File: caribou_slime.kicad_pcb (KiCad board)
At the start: 2 copper layers, 36.1 x 28.4 mm, 12 parts, among them J1 Conn_01x02_MountingPin, U1 ESP32-C3_SUPERMINI, U2 BMI270, U3 TP4056

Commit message: docs(pcb): Update silkscreen version number
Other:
- board text added: "Caribou Slime V1.1 By Pon Pon"
- board text removed: "Caribou Slime V1.0.1 By Pon Pon"
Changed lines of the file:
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@@
   (gr_rect (start 33.274 25.654) (end 69.342 54.102)
     (stroke (width 0.1) (type default)) (fill none) (layer "Edge.Cuts"))
-  (gr_text "Caribou Slime\nV1.0.1\nBy Pon Pon" (at 68.834 42.418) (layer "B.SilkS")
+  (gr_text "Caribou Slime\nV1.1\nBy Pon Pon" (at 68.834 42.418) (layer "B.SilkS")
     (effects (font (size 1 1) (thickness 0.15)) (justify left bottom mirror))
   )

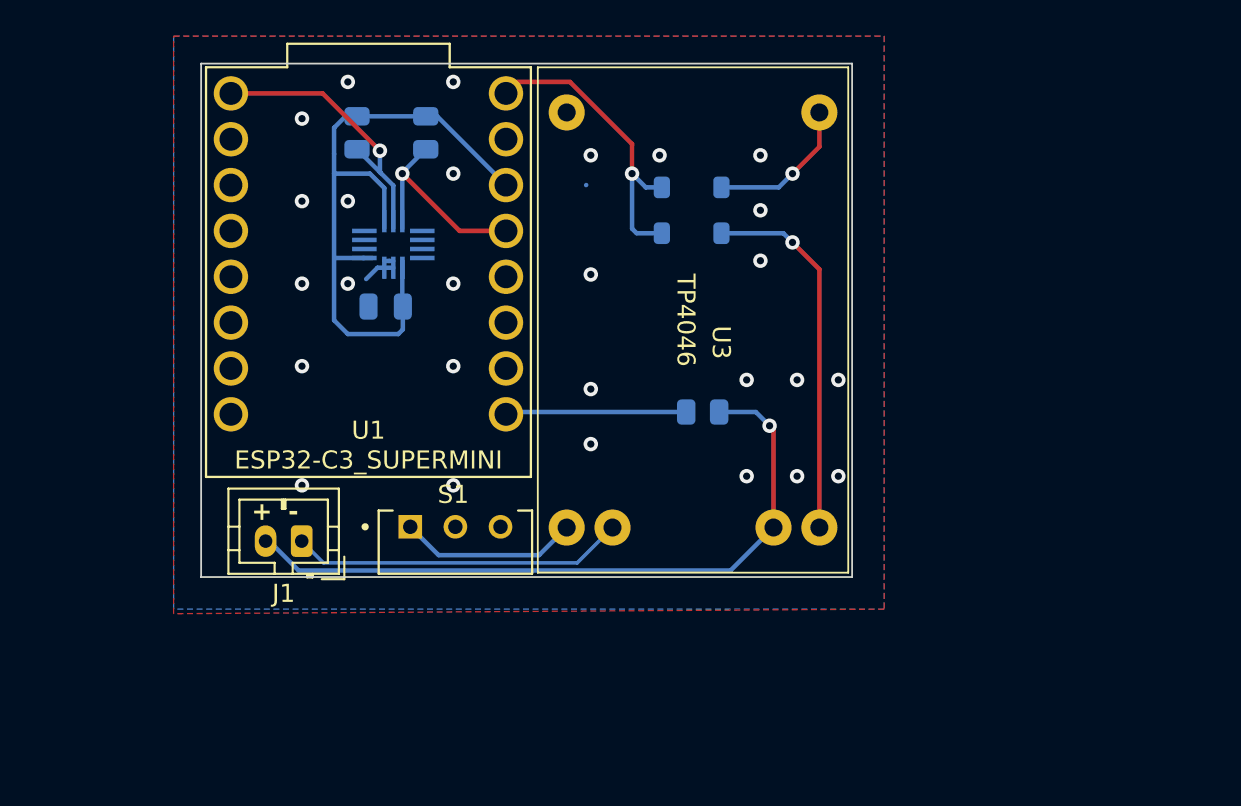
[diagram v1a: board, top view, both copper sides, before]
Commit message: chore(pcb): Remove TP4056 board
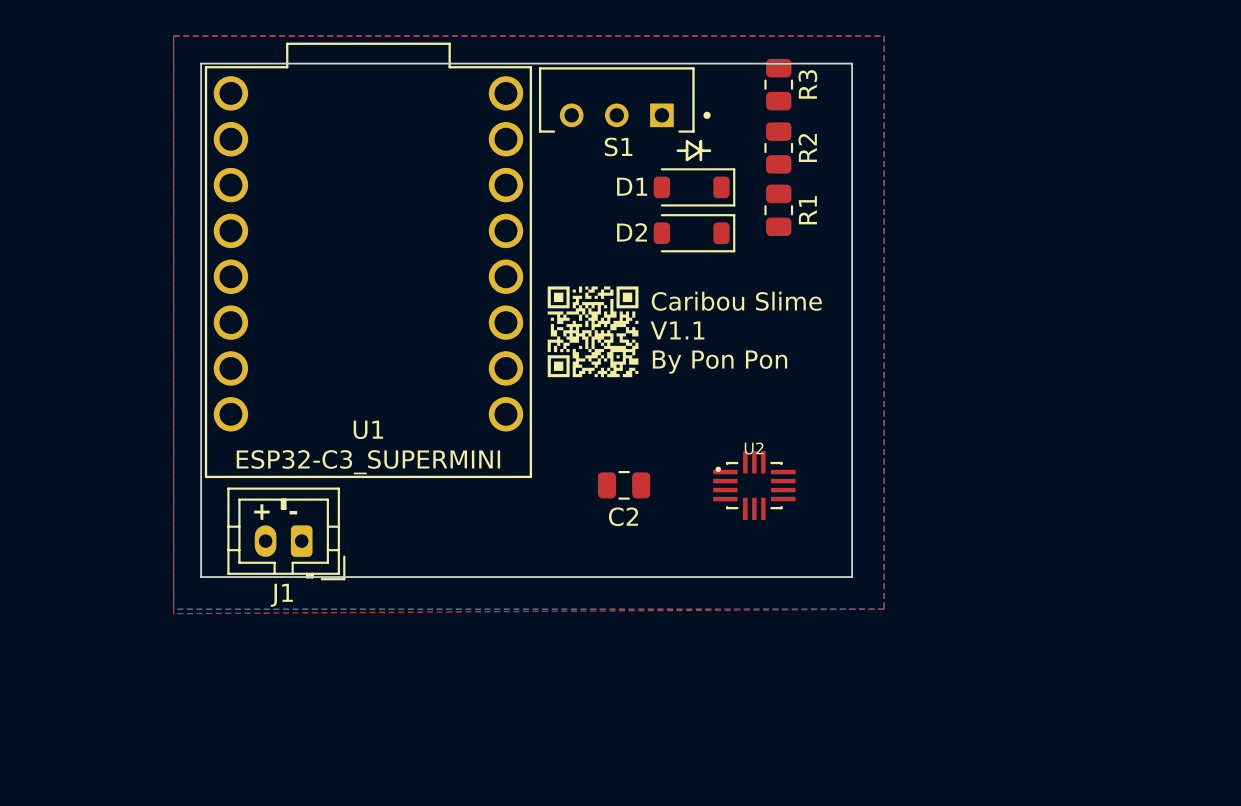
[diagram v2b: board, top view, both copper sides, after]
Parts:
- removed U3: TP4056, TP4056_Charging_Board:TP4056 Charging Board
- C2, D1, D2, G***, R1, R2, R3, U2: moved to F.Cu
- moved S1 24.5 mm to (56.3, 28.5), turned to 180 degrees
- moved U2 24.1 mm to (63.9, 49.0), turned to 0 degrees
- moved R1 23.8 mm to (65.3, 33.8)
- moved R2 19.6 mm to (65.3, 30.3)
- moved R3 18.6 mm to (65.3, 26.8), turned to -90 degrees
- moved C2 16.5 mm to (56.7, 49.0), turned to 0 degrees
- turned D1 to 180 degrees
- turned D2 to 180 degrees
- turned G*** to 0 degrees
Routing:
- net /B+: track 38.6 -> 0.00 mm, vias 1 -> 0
- net +3V3: track 37.6 -> 0.00 mm
- net Net-(D2-A): track 20.6 -> 0.00 mm, vias 1 -> 0
- net /B-: track 18.5 -> 0.00 mm
- net +5V: track 17.1 -> 0.00 mm, vias 1 -> 0
- net SCL: track 16.0 -> 0.00 mm, vias 1 -> 0
- net SDA: track 12.0 -> 0.00 mm, vias 1 -> 0
- net Net-(U1-GPIO0): track 10.0 -> 0.00 mm
- net Net-(U3-OUT-): track 9.95 -> 0.00 mm
- net Net-(D1-A): track 8.26 -> 0.00 mm, vias 1 -> 0
- net GND: track 2.27 -> 0.00 mm, vias 27 -> 0

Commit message: refactor(pcb): Design V1 PCB for Hyperion
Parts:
- removed G***: LOGO, LOGO
- added C1: 100nF, Capacitor_SMD:C_0805_2012Metric, F.Cu at (59.7, 39.0)
- added H1: B+, Connector_PinHeader_2.54mm:PinHeader_1x01_P2.54mm_Vertical, F.Cu at (75.6, 33.4)
- added H2: B-, Connector_PinHeader_2.54mm:PinHeader_1x01_P2.54mm_Vertical, F.Cu at (75.6, 31.4)
- added U3: TP4056, TP4056_Charging_Board:TP4056 Charging Board, F.Cu at (87.7, 63.9)
- moved S1 24.5 mm to (61.4, 52.5), turned to 0 degrees
- moved U2 17.9 mm to (61.0, 31.3)
- moved R3 15.0 mm to (53.7, 36.3), turned to 0 degrees
- moved U1 14.8 mm to (39.0, 51.6), turned to 180 degrees
- moved D1 13.7 mm to (68.6, 43.6), turned to -90 degrees
- moved R1 12.3 mm to (53.7, 29.7), turned to 180 degrees
- moved R2 11.9 mm to (53.7, 33.0), turned to 180 degrees
- moved C2 11.4 mm to (62.2, 39.0), turned to -90 degrees
- moved D2 8.55 mm to (68.6, 37.7), turned to 90 degrees
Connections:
- R3 pad 2: /B+ -> Net-(U3-B+)
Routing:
- net +3V3: track 0.00 -> 84.6 mm, vias 0 -> 3
- net +5V: track 0.00 -> 65.7 mm, vias 0 -> 2
- net Net-(U3-OUT-): track 0.00 -> 49.6 mm
- net SDA: track 0.00 -> 45.6 mm, vias 0 -> 1
- net /B+: track 0.00 -> 43.4 mm, vias 0 -> 1
- net unconnected-(U2-ASDX-Pad2): track 0.00 -> 27.2 mm, vias 0 -> 1
- net unconnected-(S1-Pad3): track 0.00 -> 26.4 mm
- net Net-(D1-A): track 0.00 -> 18.6 mm
- net unconnected-(U2-INT2-Pad9): track 0.00 -> 12.8 mm
- net Net-(D2-A): track 0.00 -> 5.63 mm
- net GND: track 0.00 -> 3.23 mm, vias 0 -> 34
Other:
- board size 36.1 x 28.4 mm -> 62.8 x 37.6 mm
- board text added: "Modified to Caribou Slime V1 By Pon Pon"
- board text removed: "+"
- board text removed: "-"
- board text removed: "Caribou Slime V1.1 By Pon Pon"

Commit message: docs(pcb): Correct attribution and diode silkscreen
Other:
- board text added: "Modified to Caribou Slime V1.0 By Pon Pon"
- board text removed: "Modified to Caribou Slime V1 By Pon Pon"

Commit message: fix(pcb): Add correct JST schematic and footprint
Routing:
- net unconnected-(U3---Pad2): track 0.00 -> 43.4 mm, vias 0 -> 1
- net /B+: track 43.4 -> 0.00 mm, vias 1 -> 0
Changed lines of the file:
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@@
   (net 25 "Net-(U3-OUT-)")
   (net 26 "unconnected-(S1-Pad3)")
-  (net 27 "/B+")
-  (net 28 "/B-")
+  (net 27 "unconnected-(U3---Pad2)")
+  (net 28 "/B+")
+  (net 29 "/B-")
   (footprint "Connector_JST:JST_PH_B2B-PH-K_1x02_P2.00mm_Vertical" (layer "F.Cu")
     (at 38.846 52.112 180)
@@
       (stroke (width 0.1) (type solid)) (layer "F.Fab"))
     (pad "1" thru_hole roundrect (at 0 0 180) (size 1.2 1.75) (drill 0.75) (layers "*.Cu" "*.Mask") (roundrect_rratio 0.208333)
-      (net 28 "/B-") (pinfunction "Pin_1") (pintype "passive"))
+      (net 29 "/B-") (pinfunction "Pin_1") (pintype "passive"))
     (pad "2" thru_hole oval (at 2 0 180) (size 1.2 1.75) (drill 0.75) (layers "*.Cu" "*.Mask")
-      (net 27 "/B+") (pinfunction "Pin_2") (pintype "passive"))
+      (net 28 "/B+") (pinfunction "Pin_2") (pintype "passive"))
     (model "${KICAD6_3DMODEL_DIR}/Connector_JST.3dshapes/JST_PH_B2B-PH-K_1x02_P2.00mm_Vertical.wrl"
       (offset (xyz 0 0 0))

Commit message: chore(pcb): Clear PCB for rework
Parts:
- removed H1: B+, Connector_PinHeader_2.54mm:PinHeader_1x01_P2.54mm_Vertical
- removed H2: B-, Connector_PinHeader_2.54mm:PinHeader_1x01_P2.54mm_Vertical
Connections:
- R1 pad 2: SCL -> (no net)
- R2 pad 2: SDA -> (no net)
- R3 pad 1: Net-(U1-GPIO0) -> (no net)
- R3 pad 2: Net-(U3-B+) -> (no net)
- S1 pad 1: Net-(U3-OUT-) -> (no net)
- S1 pad 3: unconnected-(S1-Pad3) -> (no net)
- U1 pad 0: Net-(U1-GPIO0) -> (no net)
- U1 pad 4: SDA -> (no net)
- U1 pad 5: SCL -> (no net)
- U2 pad 10: unconnected-(U2-OSCB-Pad10) -> (no net)
- U2 pad 11: unconnected-(U2-OSDO-Pad11) -> (no net)
- U2 pad 13: SCL -> (no net)
- U2 pad 14: SDA -> (no net)
- U2 pad 2: unconnected-(U2-ASDX-Pad2) -> (no net)
- U2 pad 3: unconnected-(U2-ASCX-Pad3) -> (no net)
- U2 pad 4: unconnected-(U2-INT1-Pad4) -> (no net)
- U2 pad 9: unconnected-(U2-INT2-Pad9) -> (no net)
- U3 pad 2: unconnected-(U3---Pad2) -> (no net)
- U3 pad 4: Net-(U3-OUT-) -> (no net)
- U3 pad 5: Net-(U3-B+) -> (no net)
- U3 pad 6: Net-(U3-B-) -> (no net)
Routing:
- net +3V3: track 84.6 -> 2.66 mm, vias 3 -> 0
- net +5V: track 65.7 -> 0.00 mm, vias 2 -> 0
- net Net-(U3-OUT-): track 49.6 -> 0.00 mm
- net SDA: track 45.6 -> 0.00 mm, vias 1 -> 0
- net unconnected-(U3---Pad2): track 43.4 -> 0.00 mm, vias 1 -> 0
- net unconnected-(U2-ASDX-Pad2): track 27.2 -> 0.00 mm, vias 1 -> 0
- net unconnected-(S1-Pad3): track 26.4 -> 0.00 mm
- net Net-(D1-A): track 18.6 -> 0.00 mm
- net unconnected-(U2-INT2-Pad9): track 12.8 -> 0.00 mm
- net Net-(D2-A): track 5.63 -> 0.00 mm
- net GND: track 3.23 -> 0.00 mm, vias 34 -> 4

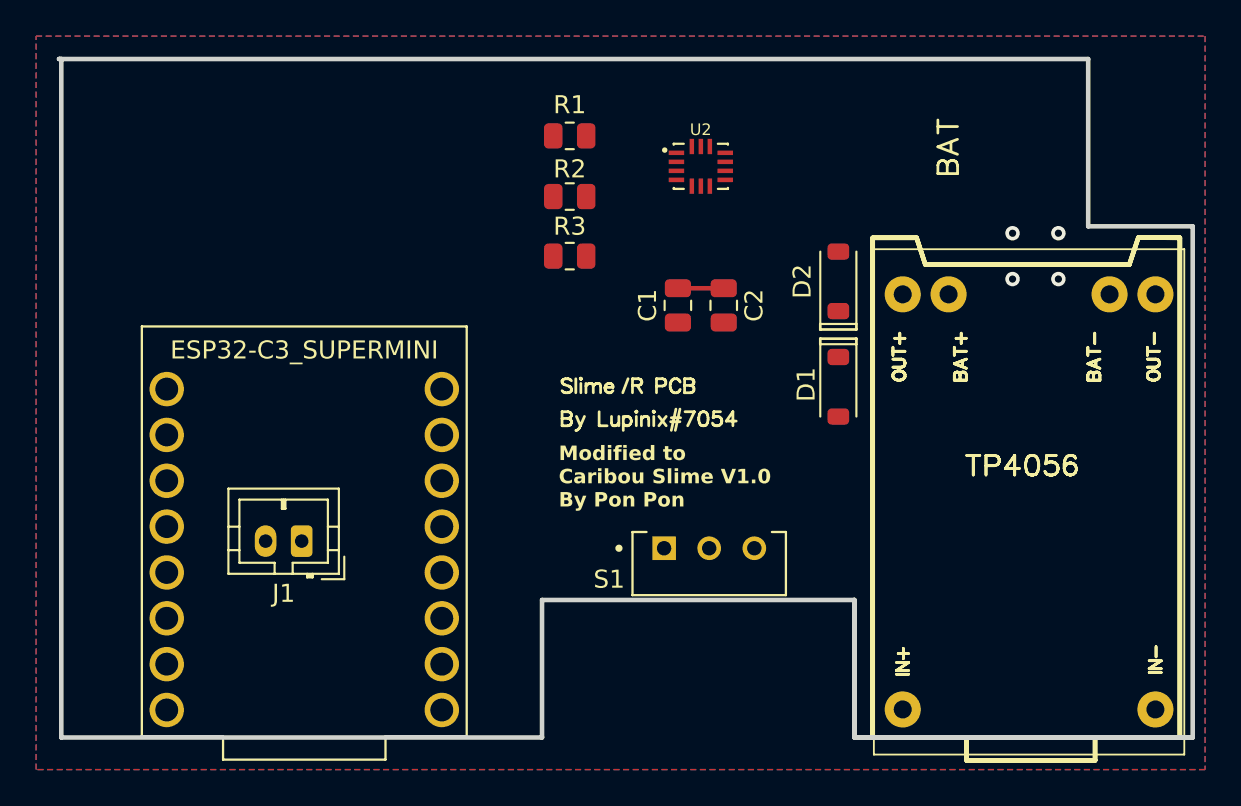
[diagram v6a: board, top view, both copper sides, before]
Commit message: docs(pcb): Prep silk screen for V1.1 Hyperion layout
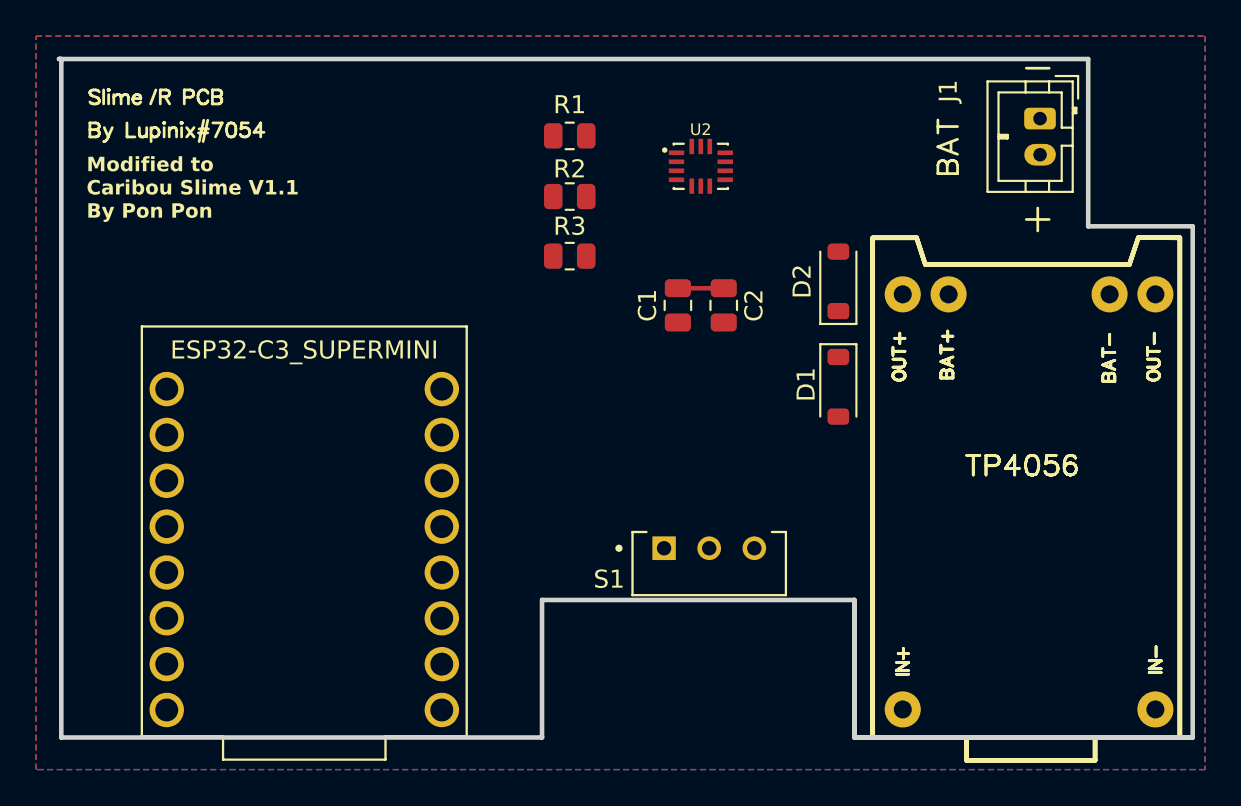
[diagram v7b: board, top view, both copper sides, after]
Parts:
- moved J1 47.1 mm to (79.8, 28.7), turned to -90 degrees
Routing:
- net GND: vias 4 -> 0
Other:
- board text added: "Modified to Caribou Slime V1.1 By Pon Pon"
- board text removed: "Modified to Caribou Slime V1.0 By Pon Pon"

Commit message: chore(pcb): Run S1 trace
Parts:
- added R4: 180k, Resistor_SMD:R_0805_2012Metric, F.Cu at (47.1, 37.1)
- moved S1 1.60 mm to (61.4, 54.1)
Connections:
- R1 pad 2: (no net) -> SCL
- R2 pad 2: (no net) -> SDA
- R3 pad 1: (no net) -> Net-(U1-GPIO0)
- R3 pad 2: (no net) -> /B+
- S1 pad 1: (no net) -> Net-(U3-OUT-)
- S1 pad 3: (no net) -> unconnected-(S1-Pad3)
- U1 pad 0: (no net) -> Net-(U1-GPIO0)
- U1 pad 4: (no net) -> SDA
- U1 pad 5: (no net) -> SCL
- U2 pad 10: (no net) -> unconnected-(U2-OSCB-Pad10)
- U2 pad 11: (no net) -> unconnected-(U2-OSDO-Pad11)
- U2 pad 13: (no net) -> SCL
- U2 pad 14: (no net) -> SDA
- U2 pad 2: (no net) -> unconnected-(U2-ASDX-Pad2)
- U2 pad 3: (no net) -> unconnected-(U2-ASCX-Pad3)
- U2 pad 4: (no net) -> unconnected-(U2-INT1-Pad4)
- U2 pad 9: (no net) -> unconnected-(U2-INT2-Pad9)
- U3 pad 2: (no net) -> unconnected-(U3---Pad2)
- U3 pad 4: (no net) -> Net-(U3-OUT-)
- U3 pad 5: (no net) -> /B+
- U3 pad 6: (no net) -> /B-
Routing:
- net Net-(U3-OUT-): track 0.00 -> 41.5 mm
